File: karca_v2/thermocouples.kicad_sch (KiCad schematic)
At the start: 10 parts, among them J8 Screw_Terminal_01x08, U14 NUP4202, U15 NUP4202, U16 NUP4202, U17 TLV9304xD

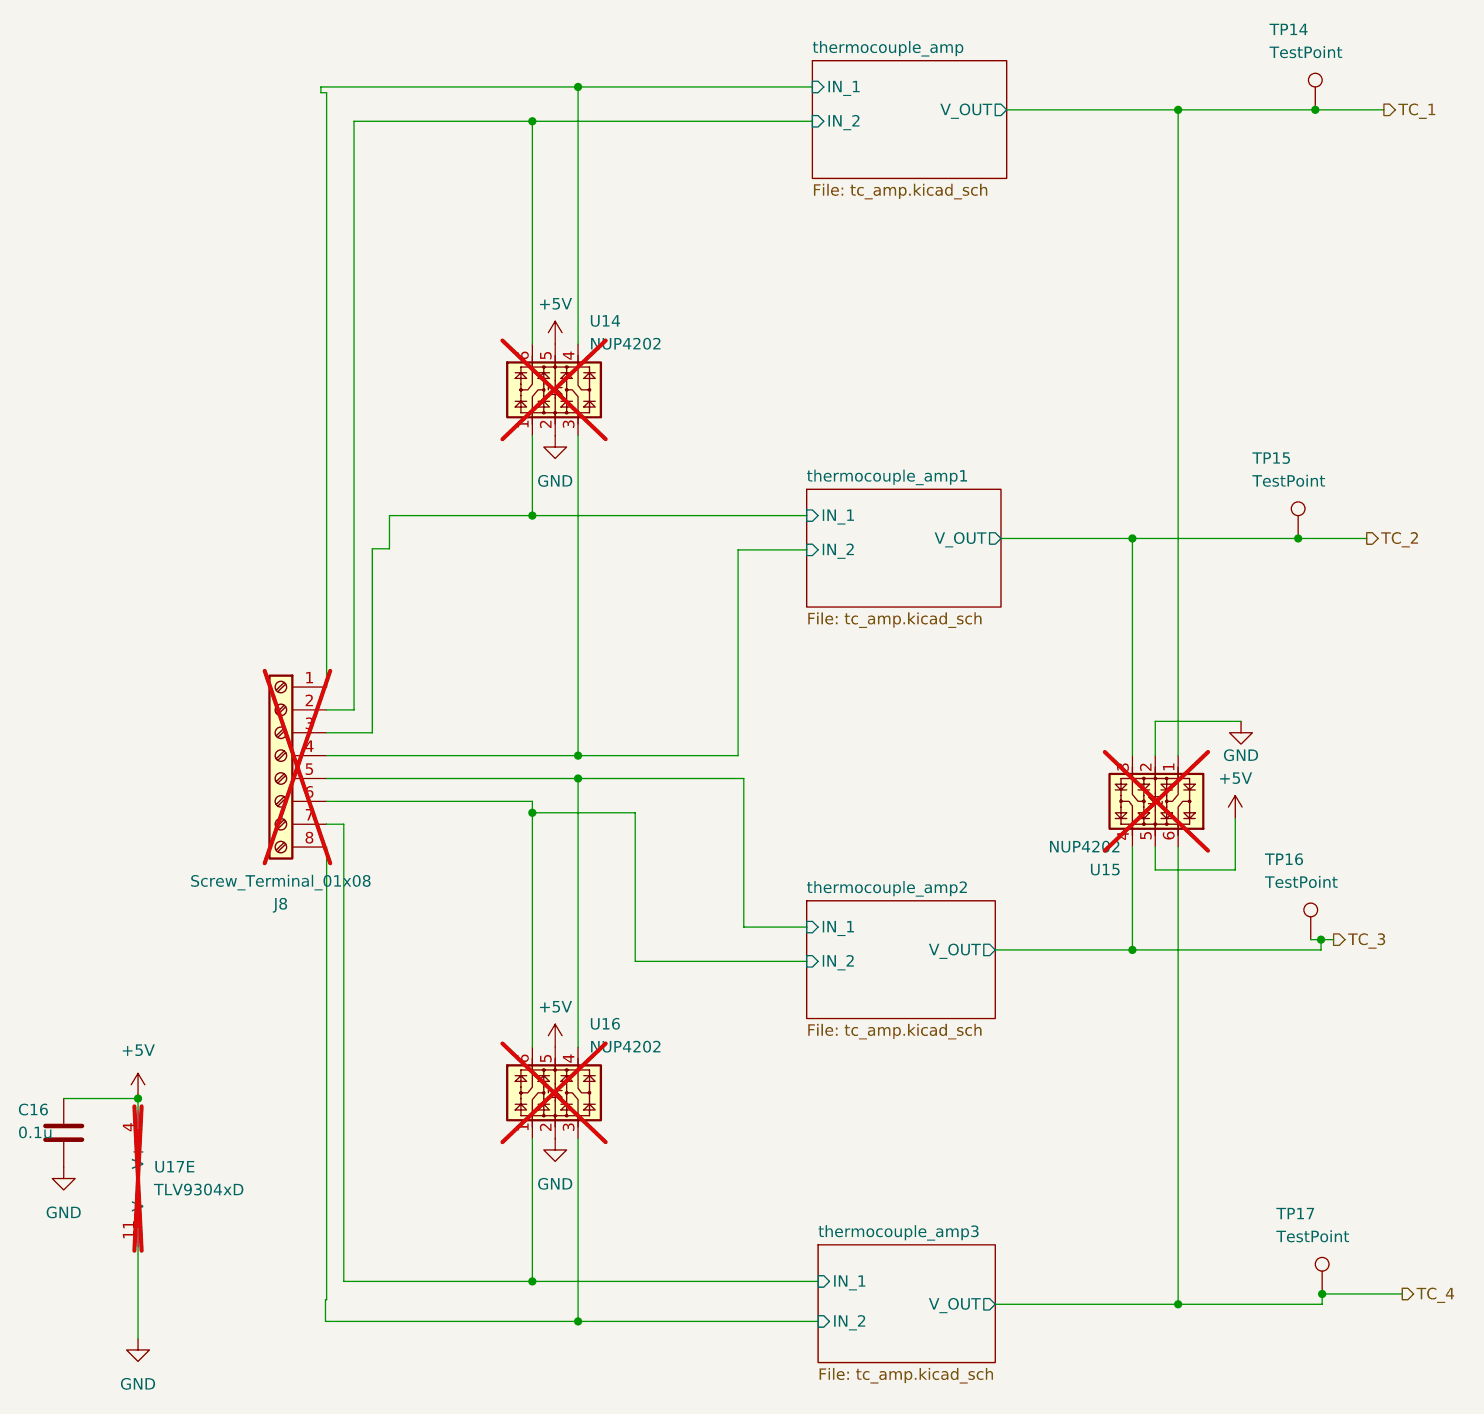
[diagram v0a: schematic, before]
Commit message: fixed all routing. Now need to clean up vias
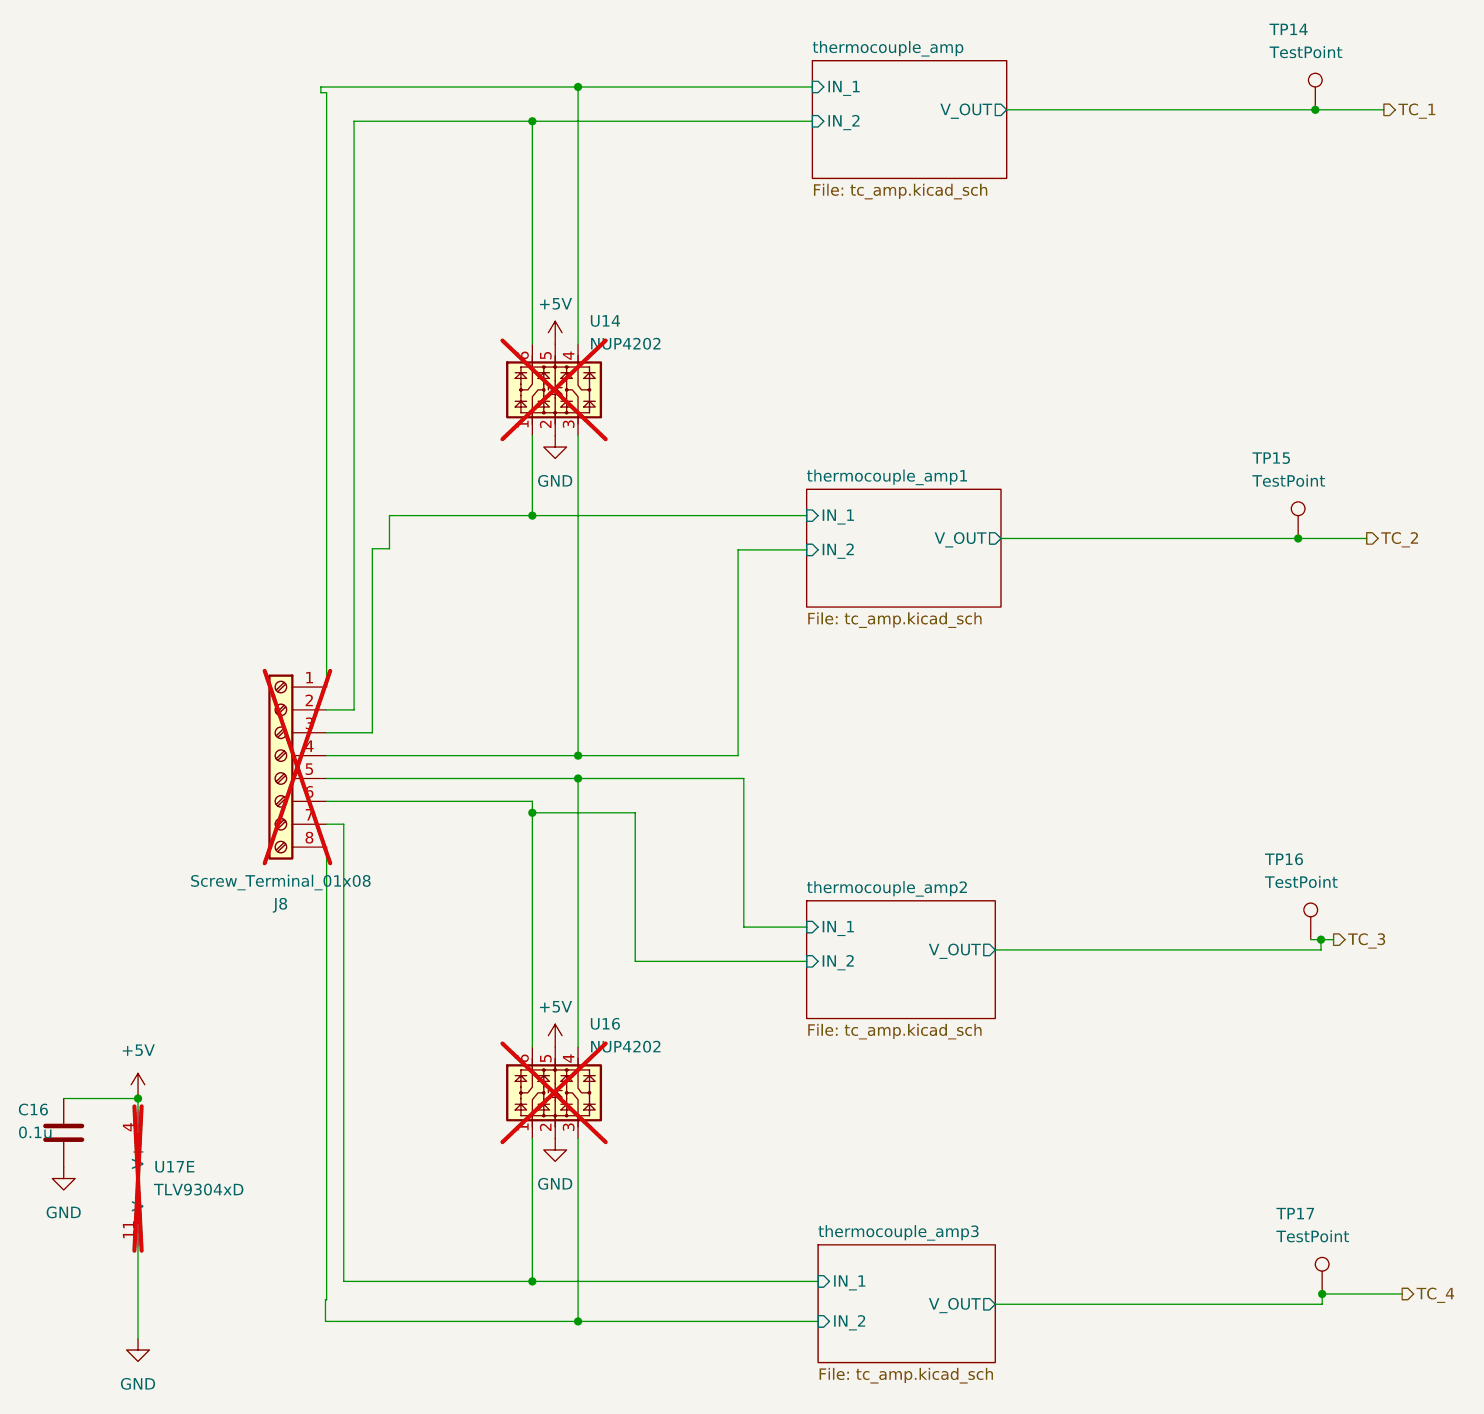
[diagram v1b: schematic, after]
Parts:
- removed U15: NUP4202, Package_TO_SOT_SMD:SOT-363_SC-70-6, symbol Power_Protection:NUP4202

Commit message: final production version
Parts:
- U14, U16, U17: now fitted; now in the parts list
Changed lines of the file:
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@@
 		(unit 5)
 		(exclude_from_sim no)
-		(in_bom no)
-		(on_board yes)
-		(dnp yes)
+		(in_bom yes)
+		(on_board yes)
+		(dnp no)
 		(fields_autoplaced yes)
 		(property "Reference" "U17"
@@
 		(unit 1)
 		(exclude_from_sim no)
-		(in_bom no)
-		(on_board yes)
-		(dnp yes)
+		(in_bom yes)
+		(on_board yes)
+		(dnp no)
+		(fields_autoplaced yes)
 		(property "Reference" "U14"
-			(at 111.125 52.705 0)
+			(at 114.3 59.0549 0)
 			(effects
 				(font
@@
 		)
 		(property "Value" "NUP4202"
-			(at 111.125 55.245 0)
+			(at 114.3 61.5949 0)
 			(effects
 				(font
@@
 		(unit 1)
 		(exclude_from_sim no)
-		(in_bom no)
-		(on_board yes)
-		(dnp yes)
+		(in_bom yes)
+		(on_board yes)
+		(dnp no)
 		(property "Reference" "U16"
 			(at 111.125 130.81 0)
